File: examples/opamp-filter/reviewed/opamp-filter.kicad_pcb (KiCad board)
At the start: 2 copper layers, 58 x 42 mm, 22 parts, among them J1 IN, J2 5V, J3 OUT, U1 MCP6001R, U2 MCP6001R

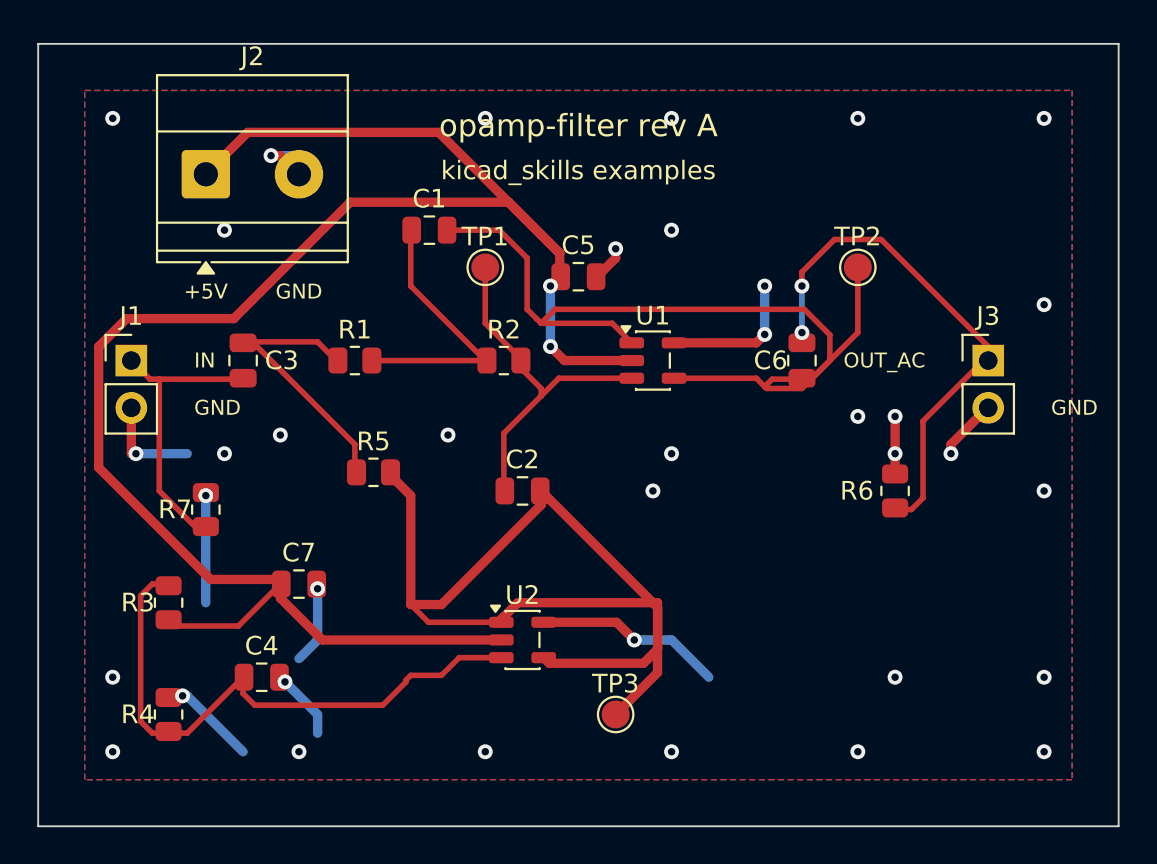
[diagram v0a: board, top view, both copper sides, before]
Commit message: Let a link finish on its own net's copper instead of the pad it names
Every junction on these boards sat on a pad, because a pad was the only
place the router was allowed to stop: a net with three branches funnelled
all three into one 0402, and the reviewer circled the result - converging
diagonals meeting on C15. People do not draw that; they tap the trunk at
the nearest point.

So the search may now end on any cell whose centre lies exactly on the
net's own copper (a tee), with two guards that took one broken board each
to learn: only copper already joined to the link's endpoint counts, or the
named pad is left unconnected; and only a pad-named endpoint may be teed
away from, because a link aimed at a bare coordinate is aimed at the
stated end of a trunk someone drew, and stopping short strands the
trunk's tail. A landing mid-segment is inserted into the trunk's points as
a stated corner, so the reshaping passes pin the join like any other.

The op-amp board shows the effect: 12% less copper, fewer corners, longer
strokes, same connectivity - DRC clean, gates clean, zero crossings on all
four regenerated boards.

Co-Authored-By: Claude Fable 5 <noreply@anthropic.com>
Claude-Session: https://claude.ai/code/session_01DUj7Ltu92tWg159mCSacwY
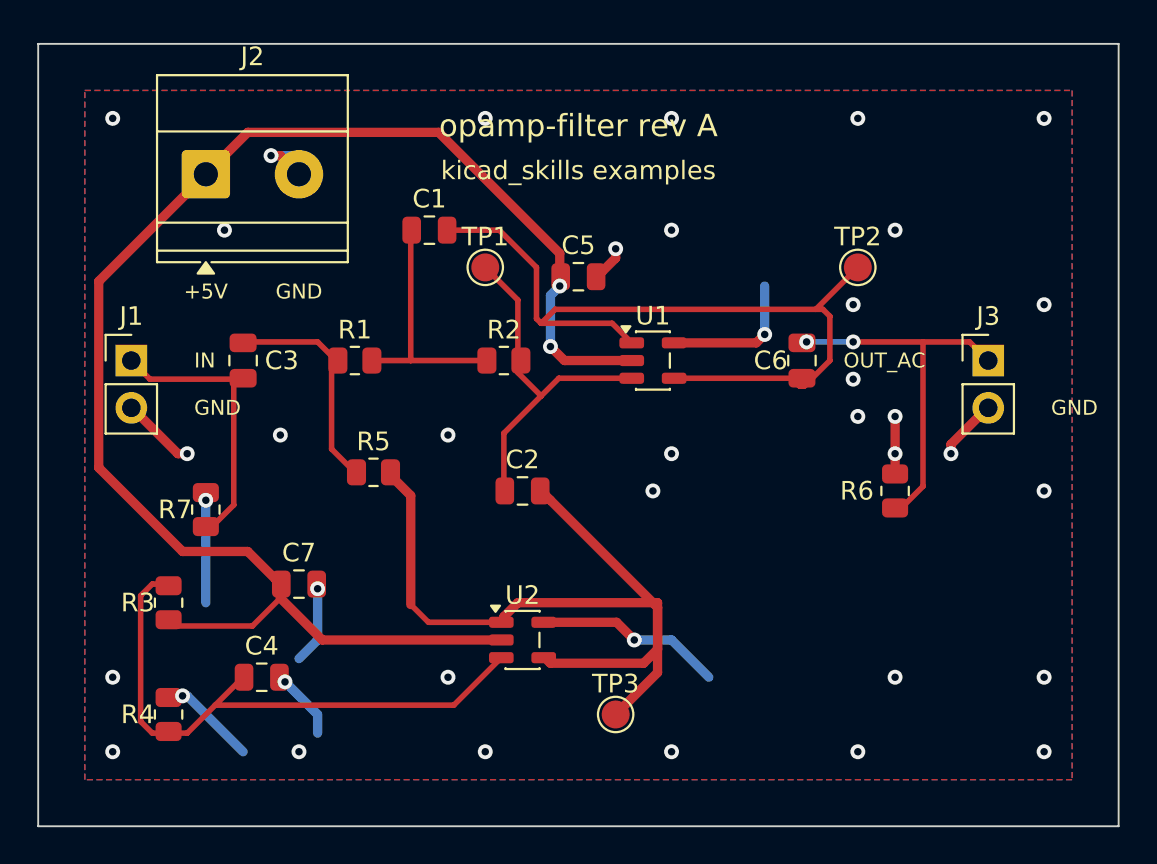
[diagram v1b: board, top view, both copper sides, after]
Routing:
- net +5V: track 101.6 -> 83.4 mm
- net /VREF: track 56.3 -> 46.3 mm
- net /OUT_AC: track 28.4 -> 20.2 mm
- net /OUT: track 50.7 -> 44.7 mm
- net /IN_DC: track 15.1 -> 12.4 mm
- net /X: track 14.9 -> 13.2 mm
- net GND: track 54.5 -> 53.0 mm, vias 37 -> 39
- net /IN: track 15.8 -> 15.2 mm

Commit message: Treat the ground plane as part of the drawing
Six reviewer circles, five of them the plane seen from different corners.
The pour now stops 1.2 mm inside the outline so an edge-hugging trace
keeps shell copper outside it; dead-end tongues narrower than 0.9 mm
retract instead of tapering to an acid-trap point in a bent corner; every
piece of the front pour over 8 mm2 holds a stitching via of its own,
placed before the orphan drop so a fenced-off strip gets a via instead of
staying a blank; and zone clearance comes down from 0.4 to 0.25, which is
what lets the plane flow between a 2.54 mm header's pins instead of
slotting the board top to bottom.

The round-twelve tee learns one manner: within two millimetres of the
goal it stands aside, so a rail flows through a bypass capacitor's pad
instead of feeding it by a stub - the carrier's bulk capacitor also moves
onto the VSYS run it was a millimetre south of. And
readability.margin_intrusion now measures symbol fields, power symbols
included: zero findings across KiCad's 18 demo sheets, one real catch on
our own motor sheet, whose power connector - like the FPGA board's -
moves in from the sheet edge so its printed name clears the frame.

Co-Authored-By: Claude Fable 5 <noreply@anthropic.com>
Claude-Session: https://claude.ai/code/session_01DUj7Ltu92tWg159mCSacwY
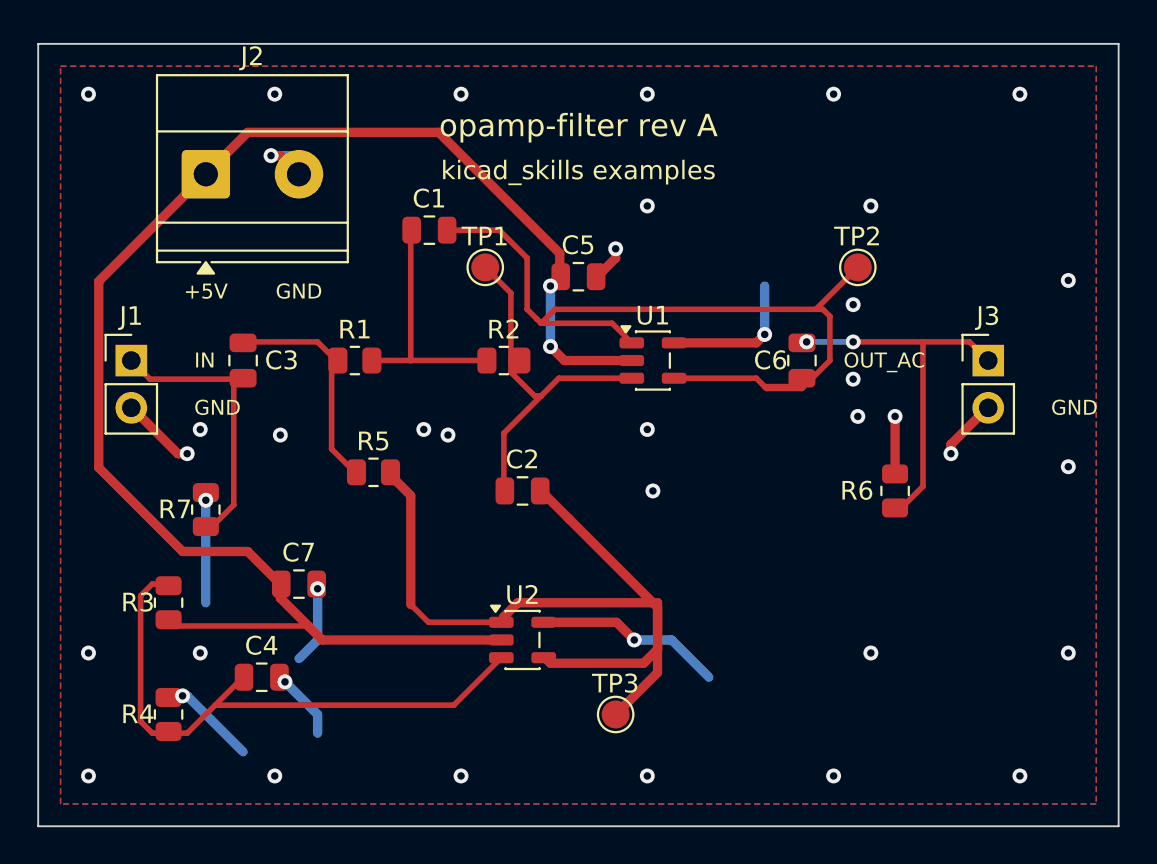
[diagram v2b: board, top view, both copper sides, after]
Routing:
- net /OUT: track 44.7 -> 47.0 mm
- net +5V: track 83.4 -> 84.3 mm
- net /FILT_IN: track 19.7 -> 20.4 mm
- net GND: vias 39 -> 40

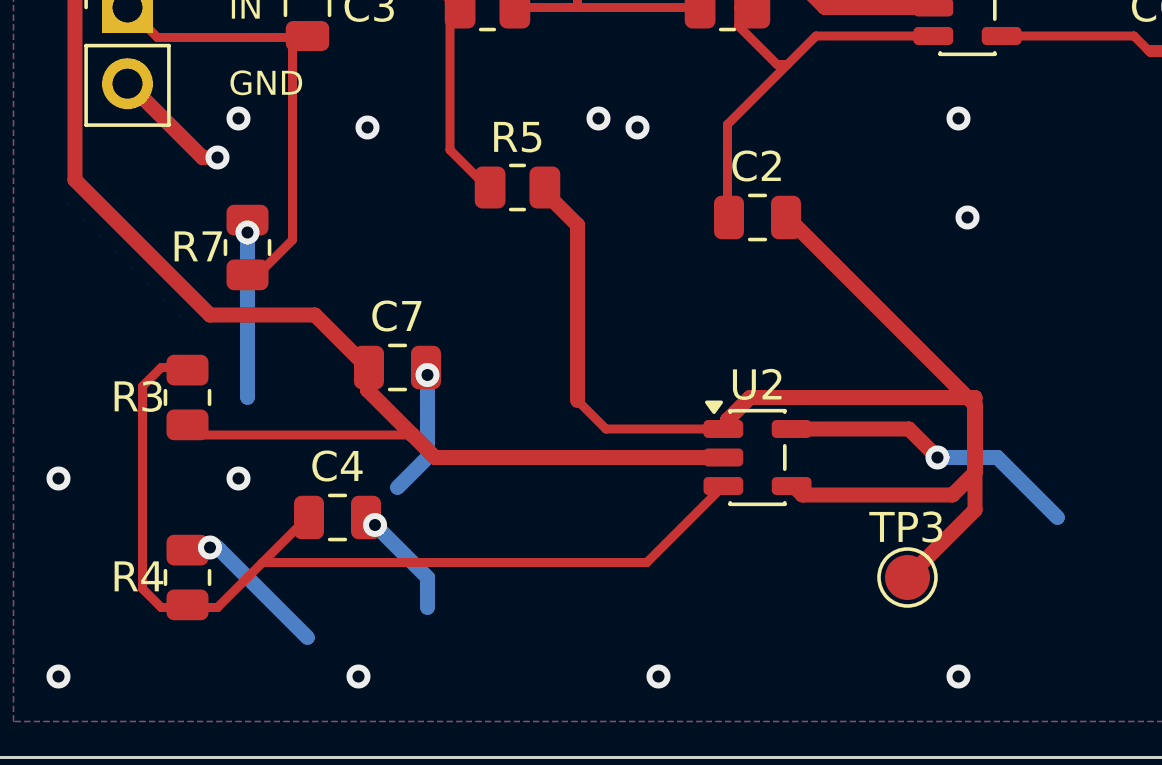
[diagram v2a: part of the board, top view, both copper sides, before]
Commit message: Regenerate the four fast boards without rides or width steps
Zero doubled runs and zero mid-run width changes across all four, by
measurement; all four pass their gates. VREF's whole run at 0.3 mm trips
track.thin_power, and the waiver answers it: the net is a buffered
half-rail loaded in microamps, the rule reads names and cannot read
currents, and the alternative was the width step the reviewer circled.

Co-Authored-By: Claude Fable 5 <noreply@anthropic.com>
Claude-Session: https://claude.ai/code/session_01DUj7Ltu92tWg159mCSacwY
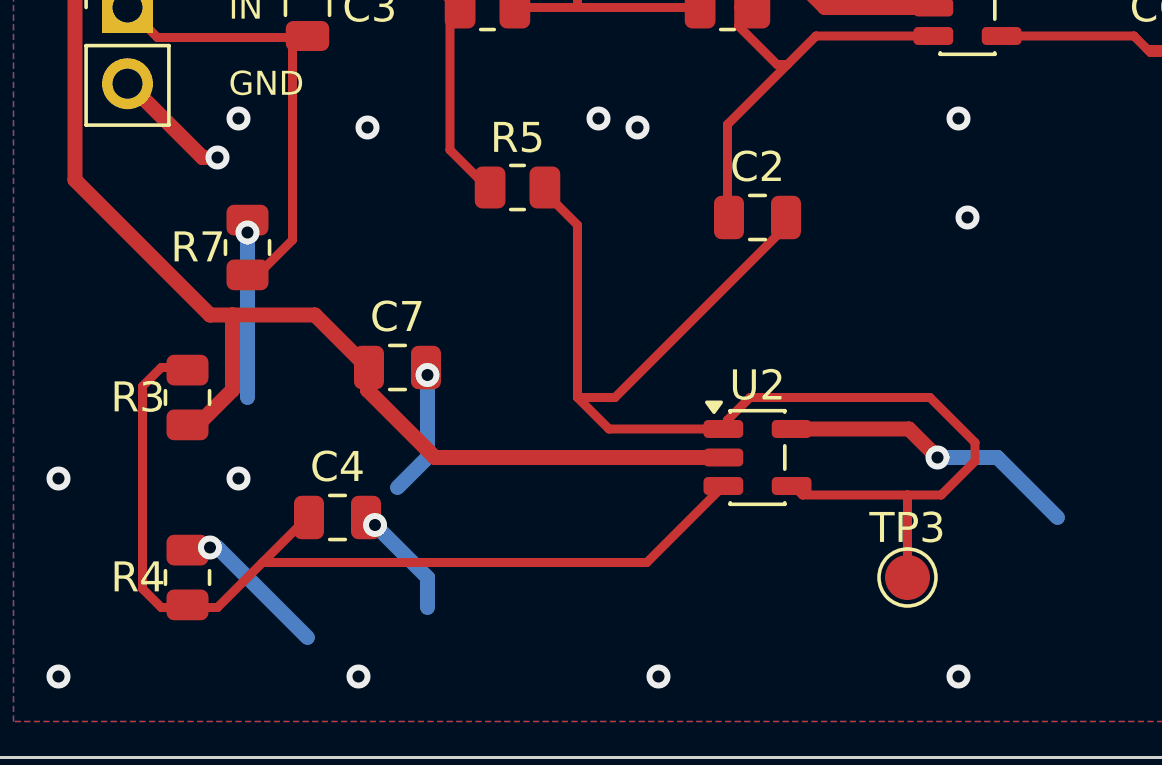
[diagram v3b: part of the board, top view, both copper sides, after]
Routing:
- net /VREF: track 46.3 -> 42.0 mm
- net +5V: track 84.3 -> 81.2 mm
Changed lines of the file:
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@@
 	(segment (start 134.1375 77.95) (end 138.55 77.95) (width 0.3) (layer "F.Cu") (net 7))
 	(segment (start 138.55 77.95) (end 139.0 78.4) (width 0.3) (layer "F.Cu") (net 7))
-	(segment (start 124.8625 91.05) (end 120.95 91.05) (width 0.3) (layer "F.Cu") (net 9))
-	(segment (start 120.95 91.05) (end 120.0 90.1) (width 0.3) (layer "F.Cu") (net 9))
+	(segment (start 131.0 93.25) (end 132.125 93.25) (width 0.3) (layer "F.Cu") (net 9))
+	(segment (start 132.125 93.25) (end 133.25 92.125) (width 0.3) (layer "F.Cu") (net 9))
+	(segment (start 133.25 92.125) (end 133.25 91.5) (width 0.3) (layer "F.Cu") (net 9))
+	(segment (start 133.25 91.5) (end 131.75 90.0) (width 0.3) (layer "F.Cu") (net 9))
+	(segment (start 131.75 90.0) (end 125.75 90.0) (width 0.3) (layer "F.Cu") (net 9))
+	(segment (start 125.75 90.0) (end 125.0 90.75) (width 0.3) (layer "F.Cu") (net 9))
+	(segment (start 125.0 90.75) (end 125.0 90.9125) (width 0.3) (layer "F.Cu") (net 9))
+	(segment (start 125.0 90.9125) (end 124.8625 91.05) (width 0.3) (layer "F.Cu") (net 9))
+	(segment (start 124.8625 91.05) (end 121.05 91.05) (width 0.3) (layer "F.Cu") (net 9))
+	(segment (start 121.05 91.05) (end 120.0 90.0) (width 0.3) (layer "F.Cu") (net 9))
 	(segment (start 124.8625 92.0) (end 115.25 92.0) (width 0.5) (layer "F.Cu") (net 2))
-	(segment (start 115.25 92.0) (end 114.5 91.25) (width 0.5) (layer "F.Cu") (net 2))
+	(segment (start 115.25 92.0) (end 113.0 89.75) (width 0.5) (layer "F.Cu") (net 2))
+	(segment (start 113.0 89.75) (end 113.0 89.25) (width 0.5) (layer "F.Cu") (net 2))
+	(segment (start 113.0 89.25) (end 113.0 89.05) (width 0.5) (layer "F.Cu") (net 2))
+	(segment (start 113.0 89.05) (end 113.025 89.025) (width 0.5) (layer "F.Cu") (net 2))
+	(segment (start 113.025 89.025) (end 113.0 89.0) (width 0.5) (layer "F.Cu") (net 2))
+	(segment (start 113.0 89.0) (end 112.75 88.75) (width 0.5) (layer "F.Cu") (net 2))
+	(segment (start 112.75 88.75) (end 111.25 87.25) (width 0.5) (layer "F.Cu") (net 2))
+	(segment (start 111.25 87.25) (end 108.5 87.25) (width 0.5) (layer "F.Cu") (net 2))
 	(segment (start 124.8625 92.95) (end 122.3125 95.5) (width 0.3) (layer "F.Cu") (net 6))
 	(segment (start 122.3125 95.5) (end 109.5 95.5) (width 0.3) (layer "F.Cu") (net 6))
@@
 	(segment (start 125.375 77.0) (end 125.375 77.625) (width 0.3) (layer "F.Cu") (net 3))
 	(segment (start 144.0 72.0) (end 141.75 74.25) (width 0.3) (layer "F.Cu") (net 7))
-	(segment (start 131.0 96.0) (end 133.25 93.75) (width 0.5) (layer "F.Cu") (net 9))
-	(segment (start 133.25 93.75) (end 133.25 90.25) (width 0.5) (layer "F.Cu") (net 9))
-	(segment (start 133.25 90.25) (end 133.0 90.0) (width 0.5) (layer "F.Cu") (net 9))
-	(segment (start 133.0 90.0) (end 128.5 85.5) (width 0.5) (layer "F.Cu") (net 9))
-	(segment (start 128.5 85.5) (end 127.25 84.25) (width 0.5) (layer "F.Cu") (net 9))
-	(segment (start 127.25 84.25) (end 127.2 84.25) (width 0.5) (layer "F.Cu") (net 9))
-	(segment (start 127.2 84.25) (end 126.95 84.0) (width 0.5) (layer "F.Cu") (net 9))
+	(segment (start 131.0 96.0) (end 131.0 93.25) (width 0.3) (layer "F.Cu") (net 9))
 	(segment (start 125.05 84.0) (end 125.05 83.8) (width 0.3) (layer "F.Cu") (net 3))
 	(segment (start 125.05 83.8) (end 125.0 83.75) (width 0.3) (layer "F.Cu") (net 3))
@@
 	(segment (start 146.25 85.0) (end 147.5 83.75) (width 0.3) (layer "F.Cu") (net 8))
 	(segment (start 147.5 83.75) (end 147.5 76.0) (width 0.3) (layer "F.Cu") (net 8))
-	(segment (start 127.1375 92.95) (end 127.2 92.95) (width 0.5) (layer "F.Cu") (net 9))
-	(segment (start 127.2 92.95) (end 127.5 93.25) (width 0.5) (layer "F.Cu") (net 9))
-	(segment (start 127.5 93.25) (end 132.5 93.25) (width 0.5) (layer "F.Cu") (net 9))
-	(segment (start 132.5 93.25) (end 133.25 92.5) (width 0.5) (layer "F.Cu") (net 9))
-	(segment (start 133.25 92.5) (end 133.25 90.0) (width 0.5) (layer "F.Cu") (net 9))
-	(segment (start 133.25 90.0) (end 133.0 90.0) (width 0.5) (layer "F.Cu") (net 9))
-	(segment (start 133.0 90.0) (end 125.75 90.0) (width 0.5) (layer "F.Cu") (net 9))
-	(segment (start 125.75 90.0) (end 125.0 90.75) (width 0.5) (layer "F.Cu") (net 9))
-	(segment (start 125.0 90.75) (end 125.0 90.9125) (width 0.5) (layer "F.Cu") (net 9))
-	(segment (start 125.0 90.9125) (end 124.8625 91.05) (width 0.5) (layer "F.Cu") (net 9))
-	(segment (start 120.0 90.1) (end 120.0 84.25) (width 0.5) (layer "F.Cu") (net 9))
-	(segment (start 120.0 84.25) (end 119.0 83.25) (width 0.5) (layer "F.Cu") (net 9))
-	(segment (start 119.0 83.25) (end 119.0 83.0875) (width 0.5) (layer "F.Cu") (net 9))
-	(segment (start 119.0 83.0875) (end 118.9125 83.0) (width 0.5) (layer "F.Cu") (net 9))
+	(segment (start 127.1375 92.95) (end 127.2 92.95) (width 0.3) (layer "F.Cu") (net 9))
+	(segment (start 127.2 92.95) (end 127.5 93.25) (width 0.3) (layer "F.Cu") (net 9))
+	(segment (start 127.5 93.25) (end 131.0 93.25) (width 0.3) (layer "F.Cu") (net 9))
+	(segment (start 120.0 90.0) (end 121.25 90.0) (width 0.3) (layer "F.Cu") (net 9))
+	(segment (start 121.25 90.0) (end 127.0 84.25) (width 0.3) (layer "F.Cu") (net 9))
+	(segment (start 127.0 84.25) (end 127.0 84.05) (width 0.3) (layer "F.Cu") (net 9))
+	(segment (start 127.0 84.05) (end 126.95 84.0) (width 0.3) (layer "F.Cu") (net 9))
+	(segment (start 120.0 90.0) (end 120.0 84.25) (width 0.3) (layer "F.Cu") (net 9))
+	(segment (start 120.0 84.25) (end 119.0 83.25) (width 0.3) (layer "F.Cu") (net 9))
+	(segment (start 119.0 83.25) (end 119.0 83.0875) (width 0.3) (layer "F.Cu") (net 9))
+	(segment (start 119.0 83.0875) (end 118.9125 83.0) (width 0.3) (layer "F.Cu") (net 9))
 	(segment (start 107.0 89.0875) (end 106.8375 89.0875) (width 0.3) (layer "F.Cu") (net 6))
 	(segment (start 106.8375 89.0875) (end 106.75 89.0) (width 0.3) (layer "F.Cu") (net 6))
@@
 	(segment (start 103.25 72.75) (end 103.25 82.75) (width 0.5) (layer "F.Cu") (net 2))
 	(segment (start 103.25 82.75) (end 107.75 87.25) (width 0.5) (layer "F.Cu") (net 2))
-	(segment (start 107.75 87.25) (end 111.25 87.25) (width 0.5) (layer "F.Cu") (net 2))
-	(segment (start 111.25 87.25) (end 112.75 88.75) (width 0.5) (layer "F.Cu") (net 2))
-	(segment (start 112.75 88.75) (end 113.0 89.0) (width 0.5) (layer "F.Cu") (net 2))
-	(segment (start 113.0 89.0) (end 113.025 89.025) (width 0.5) (layer "F.Cu") (net 2))
-	(segment (start 113.025 89.025) (end 113.0 89.05) (width 0.5) (layer "F.Cu") (net 2))
-	(segment (start 113.0 89.05) (end 113.0 89.25) (width 0.5) (layer "F.Cu") (net 2))
-	(segment (start 113.0 89.25) (end 113.0 89.75) (width 0.5) (layer "F.Cu") (net 2))
-	(segment (start 113.0 89.75) (end 114.5 91.25) (width 0.5) (layer "F.Cu") (net 2))
+	(segment (start 107.75 87.25) (end 108.5 87.25) (width 0.5) (layer "F.Cu") (net 2))
 	(segment (start 127.5 76.25) (end 127.5 73.0) (width 0.5) (layer "B.Cu") (net 2))
-	(segment (start 107.0 90.9125) (end 107.0 91.0) (width 0.3) (layer "F.Cu") (net 2))
-	(segment (start 107.0 91.0) (end 107.25 91.25) (width 0.3) (layer "F.Cu") (net 2))
-	(segment (start 107.25 91.25) (end 114.5 91.25) (width 0.3) (layer "F.Cu") (net 2))
+	(segment (start 107.0 90.9125) (end 107.1625 90.9125) (width 0.5) (layer "F.Cu") (net 2))
+	(segment (start 107.1625 90.9125) (end 107.25 91.0) (width 0.5) (layer "F.Cu") (net 2))
+	(segment (start 107.25 91.0) (end 108.5 89.75) (width 0.5) (layer "F.Cu") (net 2))
+	(segment (start 108.5 89.75) (end 108.5 87.25) (width 0.5) (layer "F.Cu") (net 2))
 	(via (at 113.0 81.0) (size 0.8) (drill 0.4) (layers "F.Cu" "B.Cu") (net 1))
 	(via (at 122.0 81.0) (size 0.8) (drill 0.4) (layers "F.Cu" "B.Cu") (net 1))
